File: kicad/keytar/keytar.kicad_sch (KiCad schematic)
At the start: 36 parts, among them J1 , J2 USB_B, J3 AudioJack2, J4 Conn_01x04, J5 USB_A, J6 Mini-DIN-6-Shielded, J7 Conn_01x04, Q1 BSS138, Q2 BSS138, SW1 SW_DPST_x2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

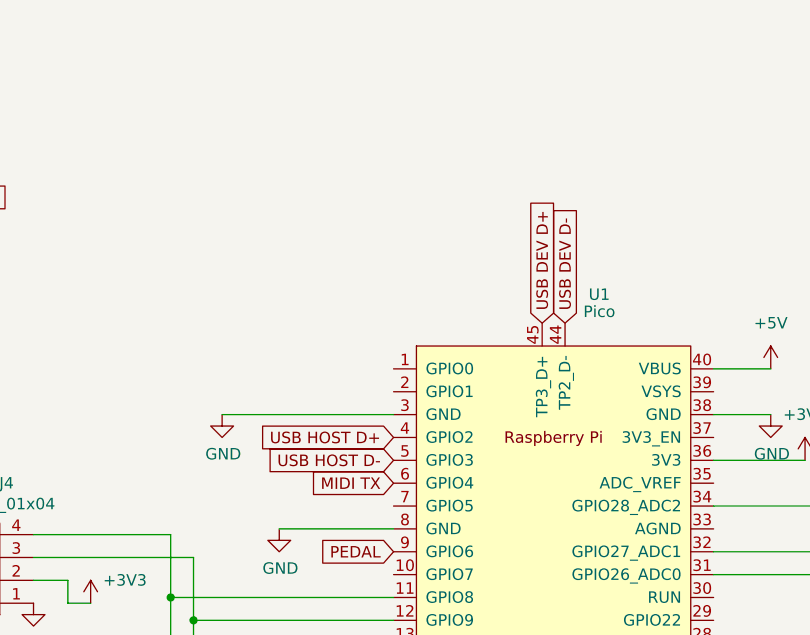
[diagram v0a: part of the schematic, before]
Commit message: pcb: switch usb device and host pins
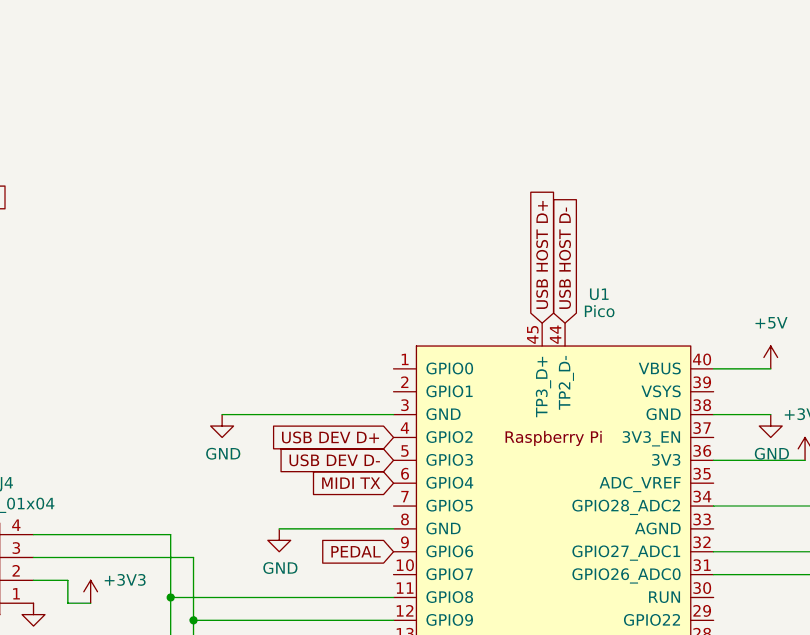
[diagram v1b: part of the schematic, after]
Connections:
- net USB DEV D+: now also U1.4 (GPIO2); no longer U1.45 (TP3_D+)
- net USB DEV D-: now also U1.5 (GPIO3); no longer U1.44 (TP2_D-)
- net USB HOST D+: now also U1.45 (TP3_D+); no longer U1.4 (GPIO2)
- net USB HOST D-: now also U1.44 (TP2_D-); no longer U1.5 (GPIO3)
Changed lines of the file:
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@@
-    )
-  )
-  (global_label "USB HOST D-" (shape input) (at 127 66.04 180) (fields_autoplaced)
-    (effects (font (size 1.27 1.27)) (justify right))
-    (property "Intersheetrefs" "${INTERSHEET_REFS}" (at 111.2433 66.04 0)
-      (effects (font (size 1.27 1.27)) (justify right) hide)
     )
   )
@@
     )
   )
-  (global_label "USB DEV D+" (shape input) (at 143.51 50.8 90) (fields_autoplaced)
+  (global_label "USB HOST D-" (shape input) (at 146.05 50.8 90) (fields_autoplaced)
     (effects (font (size 1.27 1.27)) (justify left))
-    (property "Intersheetrefs" "${INTERSHEET_REFS}" (at 143.51 36.3738 90)
+    (property "Intersheetrefs" "${INTERSHEET_REFS}" (at 146.05 35.0433 90)
       (effects (font (size 1.27 1.27)) (justify left) hide)
     )
@@
     )
   )
-  (global_label "USB HOST D+" (shape input) (at 127 63.5 180) (fields_autoplaced)
-    (effects (font (size 1.27 1.27)) (justify right))
-    (property "Intersheetrefs" "${INTERSHEET_REFS}" (at 111.2433 63.5 0)
-      (effects (font (size 1.27 1.27)) (justify right) hide)
-    )
-  )
   (global_label "MIDI TX" (shape input) (at 127 68.58 180) (fields_autoplaced)
     (effects (font (size 1.27 1.27)) (justify right))
@@
     )
   )
+  (global_label "USB DEV D+" (shape input) (at 127 63.5 180) (fields_autoplaced)
+    (effects (font (size 1.27 1.27)) (justify right))
+    (property "Intersheetrefs" "${INTERSHEET_REFS}" (at 112.5738 63.5 0)
+      (effects (font (size 1.27 1.27)) (justify right) hide)
+    )
+  )
+  (global_label "USB DEV D-" (shape input) (at 127 66.04 180) (fields_autoplaced)
+    (effects (font (size 1.27 1.27)) (justify right))
+    (property "Intersheetrefs" "${INTERSHEET_REFS}" (at 112.5738 66.04 0)
+      (effects (font (size 1.27 1.27)) (justify right) hide)
+    )
+  )
   (global_label "USB DEV D+" (shape input) (at 243.84 30.48 0) (fields_autoplaced)
     (effects (font (size 1.27 1.27)) (justify left))
@@
     (effects (font (size 1.27 1.27)) (justify left))
     (property "Intersheetrefs" "${INTERSHEET_REFS}" (at 74.8117 62.865 0)
+      (effects (font (size 1.27 1.27)) (justify left) hide)
+    )
+  )
+  (global_label "USB HOST D+" (shape input) (at 143.51 50.8 90) (fields_autoplaced)
+    (effects (font (size 1.27 1.27)) (justify left))
+    (property "Intersheetrefs" "${INTERSHEET_REFS}" (at 143.51 35.0433 90)
       (effects (font (size 1.27 1.27)) (justify left) hide)
     )
@@
     )
   )
-  (global_label "USB DEV D-" (shape input) (at 146.05 50.8 90) (fields_autoplaced)
-    (effects (font (size 1.27 1.27)) (justify left))
-    (property "Intersheetrefs" "${INTERSHEET_REFS}" (at 146.05 36.3738 90)
-      (effects (font (size 1.27 1.27)) (justify left) hide)
-    )
-  )

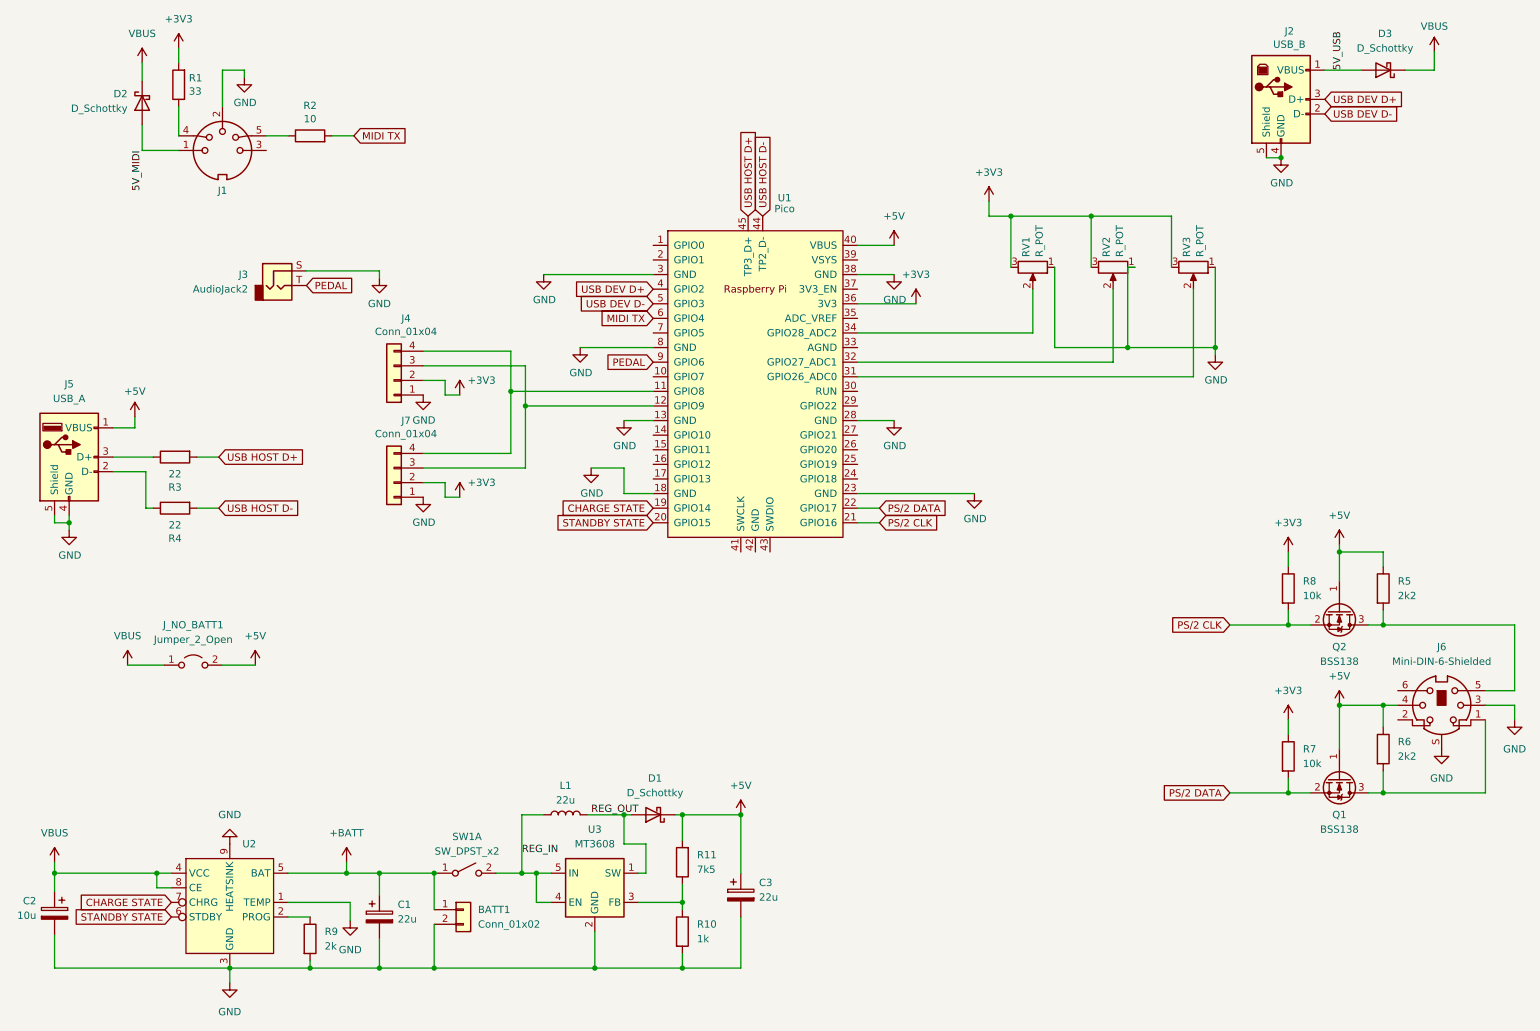
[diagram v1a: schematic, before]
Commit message: kicad: add voltage divider for battery voltage measurement
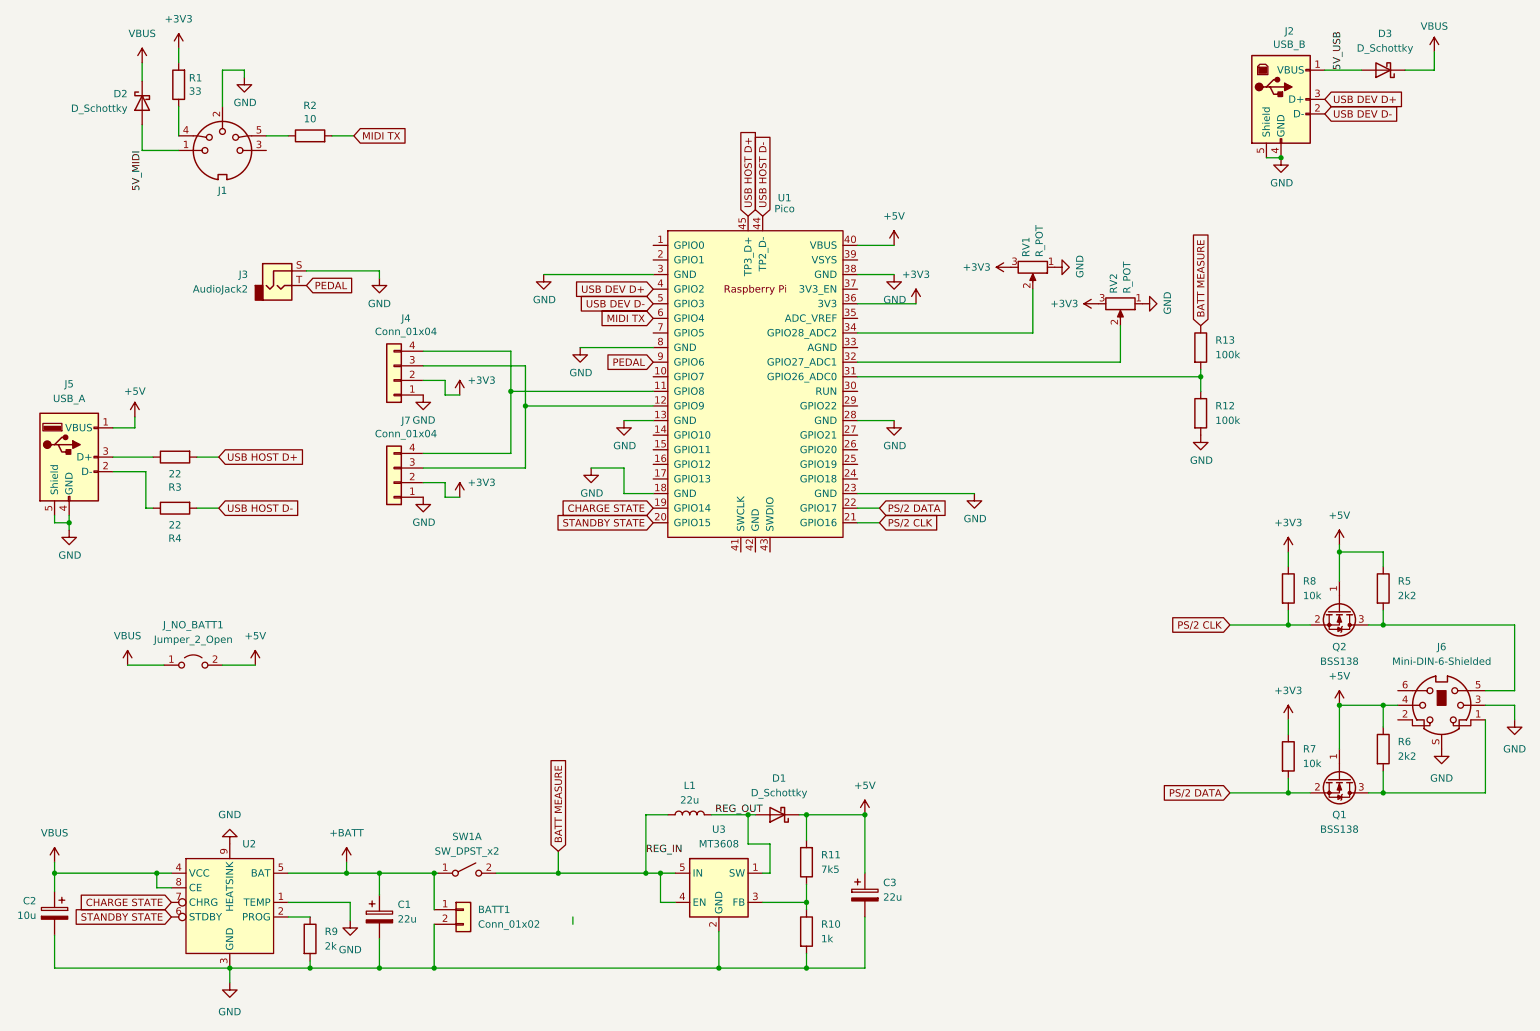
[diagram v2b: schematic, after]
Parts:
- removed RV3: R_POT, Connector_JST:JST_XH_B3B-XH-A_1x03_P2.50mm_Vertical, symbol keytar-rescue:R_POT-Device
- added R12, R13: 100k, Resistor_SMD:R_1206_3216Metric_Pad1.30x1.75mm_HandSolder, symbol Device:R
- J1: value (none) -> ~
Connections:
- net GND: now also R12.2
- net at U1.31 (GPIO26_ADC0): now also R12.1, R13.2
- net REG_IN renamed BATT MEASURE
- net BATT MEASURE: now also R13.1
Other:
- moved on the sheet: C3, D1, L1, R10, R11, RV2, U3
